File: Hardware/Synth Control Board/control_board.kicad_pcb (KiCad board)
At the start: 2 copper layers, 127 x 177.8 mm, 48 parts, among them J1 Conn_01x13, J10 Conn_01x05, J2 Conn_01x03, J3 Conn_01x13, J4 Conn_01x13, J5 Conn_01x02, J6 Conn_01x13, J7 Conn_01x05, J8 Conn_01x05, J9 Conn_01x05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

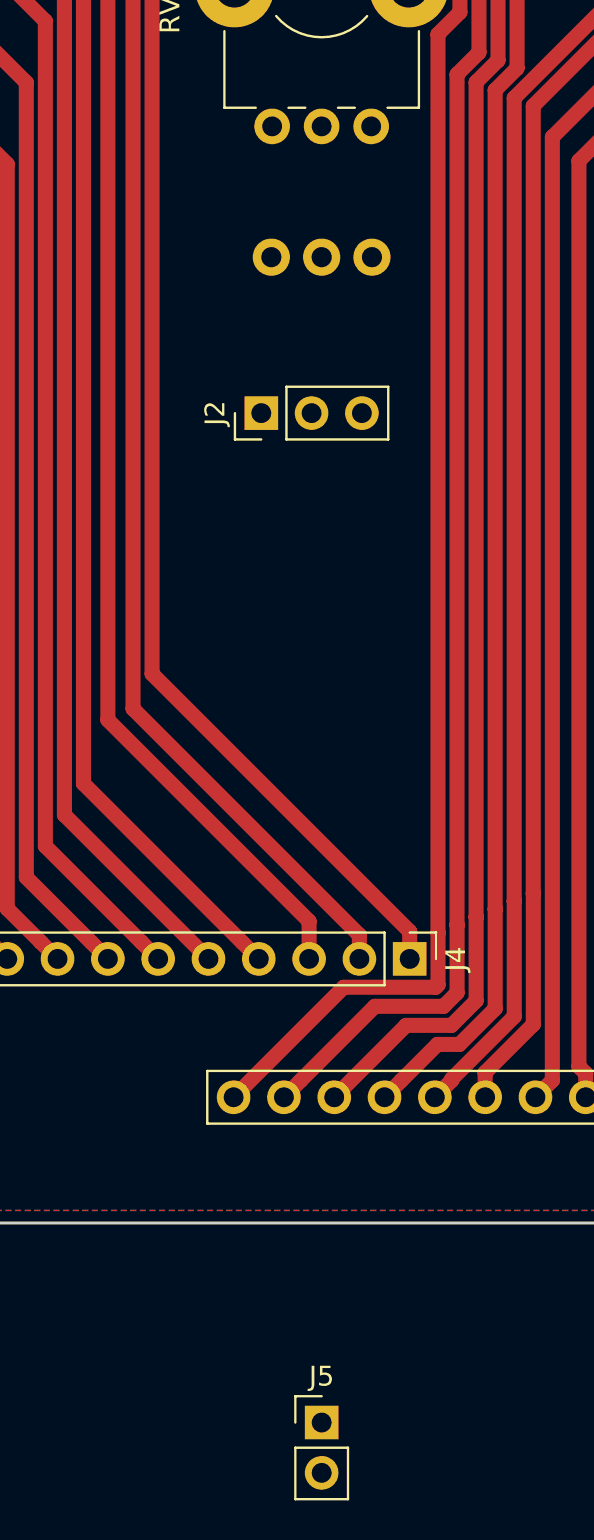
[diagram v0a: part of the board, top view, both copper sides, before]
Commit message: match relative connector placement between two boards
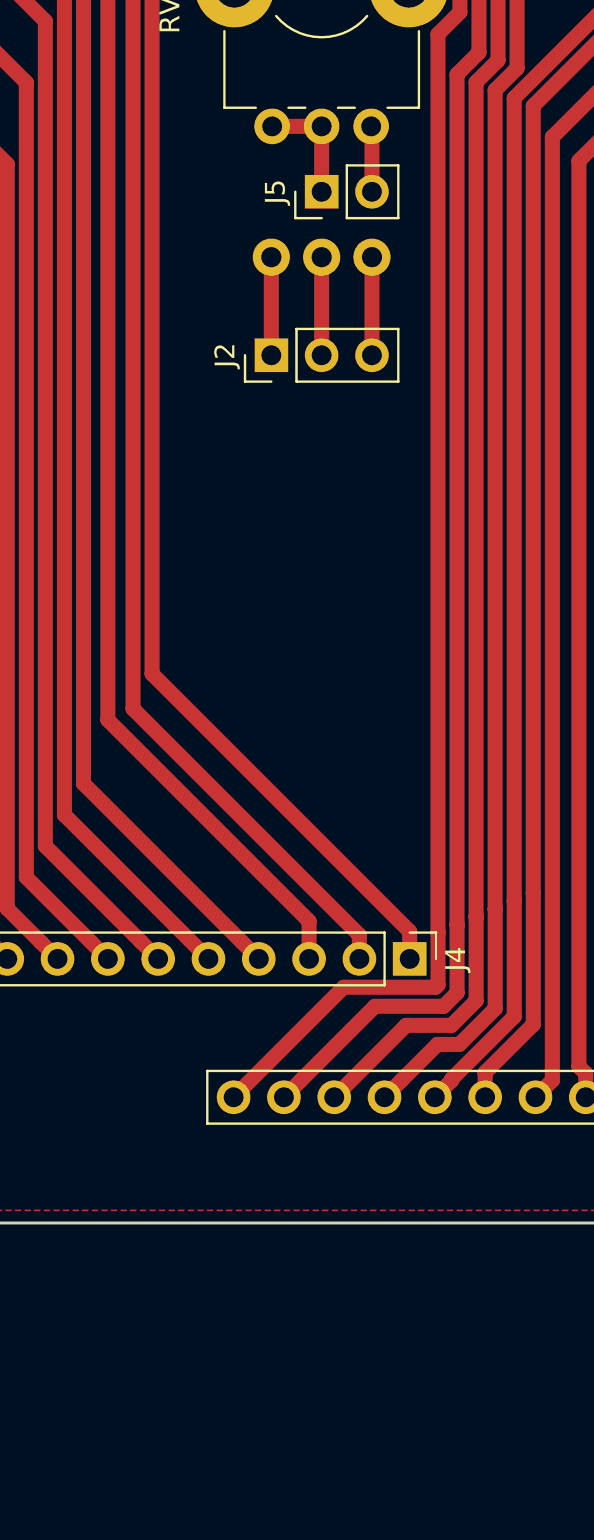
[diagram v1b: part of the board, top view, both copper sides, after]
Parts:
- moved J5 62.1 mm to (63.5, 125.7), turned to 90 degrees
- moved J2 2.96 mm to (61.0, 134.0)
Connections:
- J1 pad 13: GNDD -> GND
- J3 pad 2: GNDD -> GND
- J4 pad 13: GNDD -> GND
- J6 pad 2: GNDD -> GND
- SW10 pad 1: GNDD -> GND
- SW11 pad 1: GNDD -> GND
- SW12 pad 1: GNDD -> GND
- SW13 pad 1: GNDD -> GND
- SW6 pad 2: GNDD -> GND
- SW7 pad 2: GNDD -> GND
- SW8 pad 2: GNDD -> GND
- SW9 pad 2: GNDD -> GND
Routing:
- net /LFO_freq_in: track 0.00 -> 5.80 mm
- net /LFO_tri: track 0.00 -> 4.95 mm
- net /LFO_square: track 0.00 -> 4.95 mm
- net /LFO_out: track 0.00 -> 4.95 mm
- net /LFO_freq_out: track 0.00 -> 3.32 mm

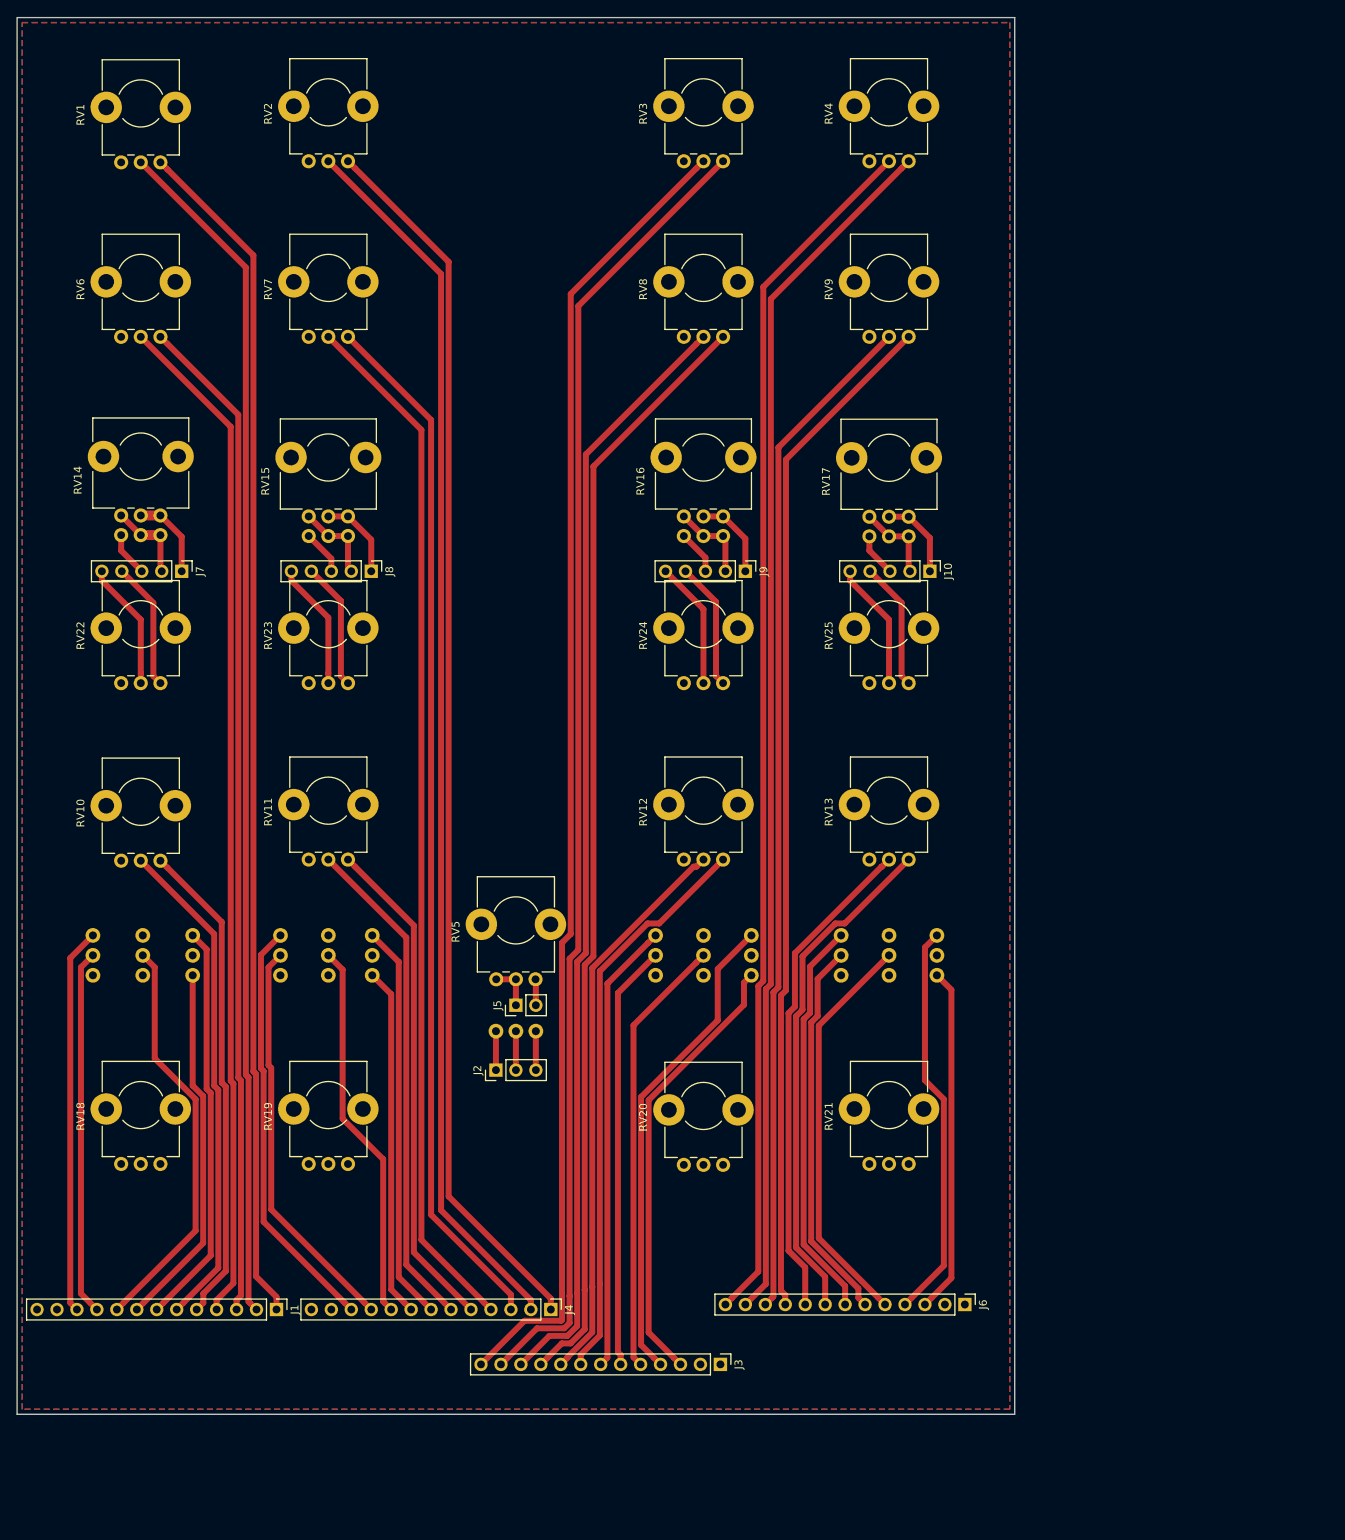
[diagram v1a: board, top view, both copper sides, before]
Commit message: add delay connector to main board and route it.
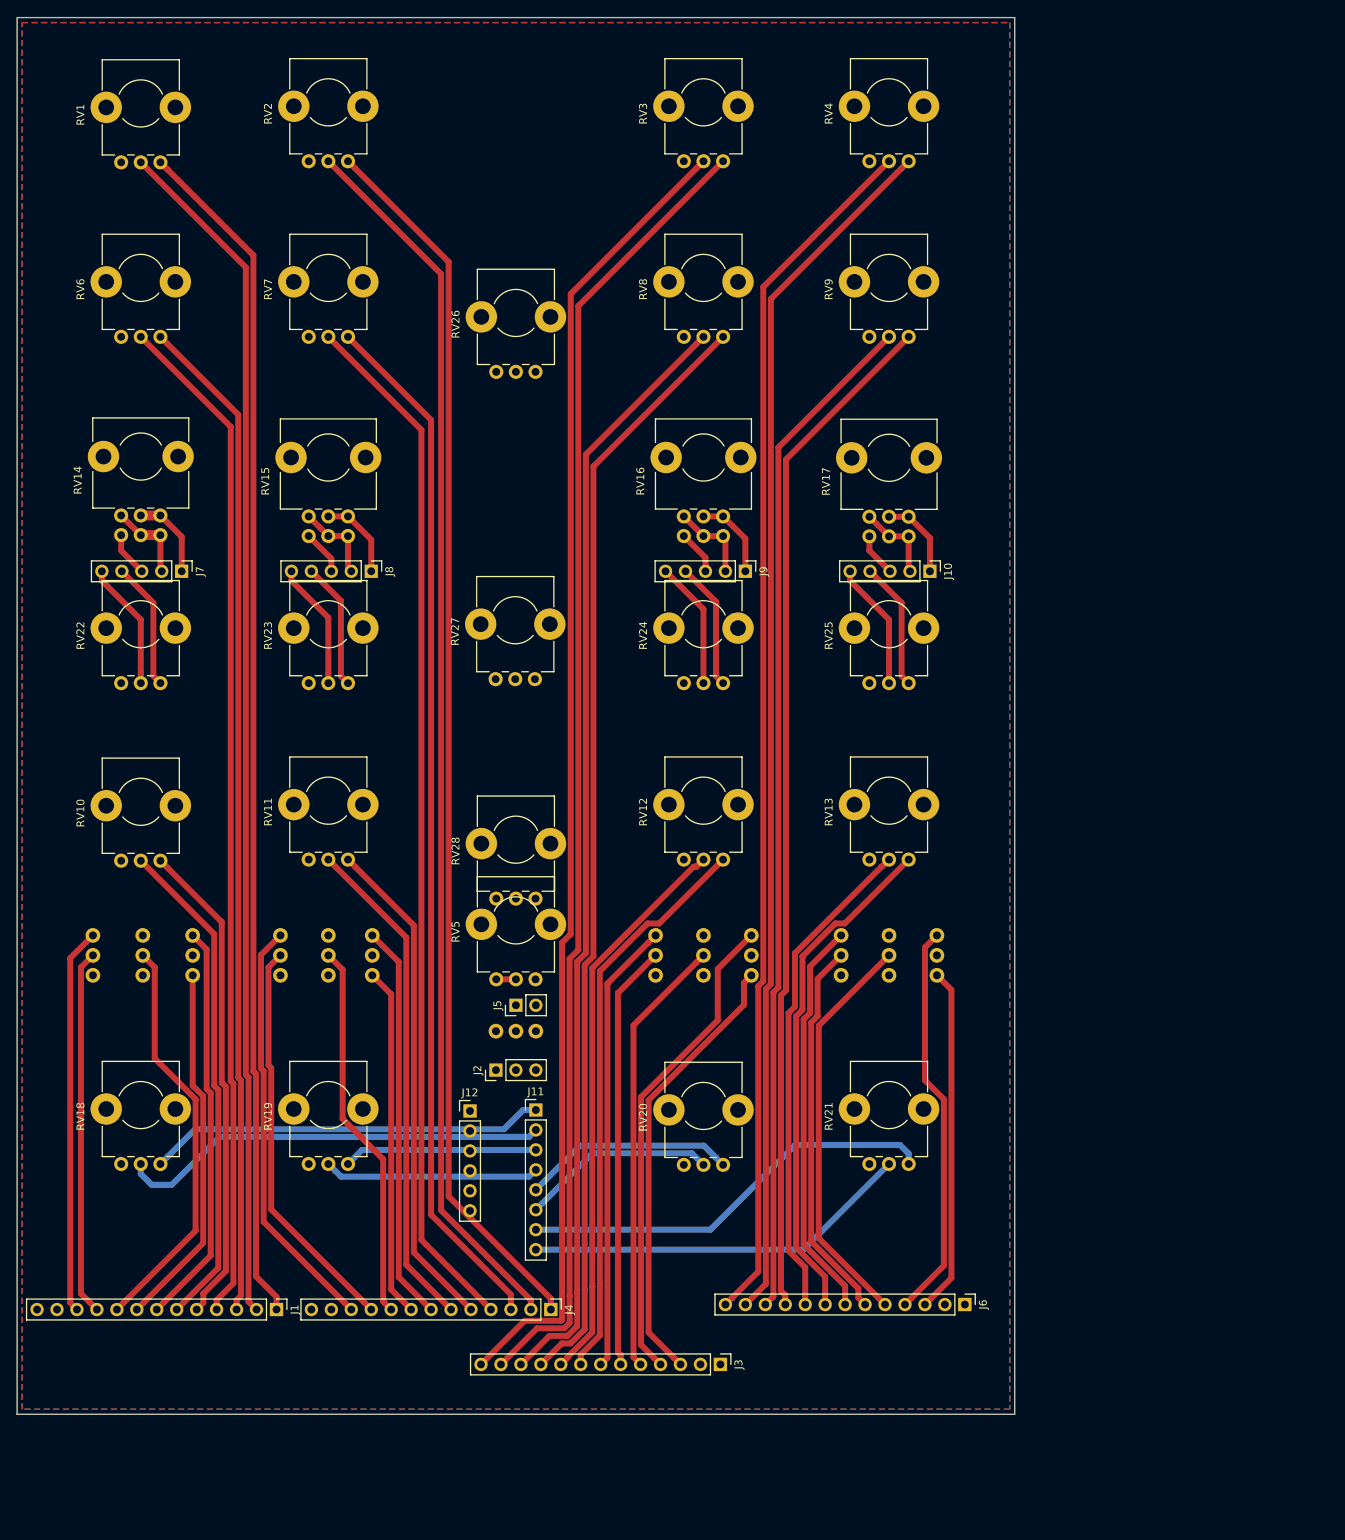
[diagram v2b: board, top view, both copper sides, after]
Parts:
- added J11: Conn_01x08, Pin_Headers:Pin_Header_Straight_1x08_Pitch2.54mm, F.Cu at (66.0, 139.1)
- added J12: Conn_01x06, Pin_Headers:Pin_Header_Straight_1x06_Pitch2.54mm, F.Cu at (57.7, 139.2)
- added RV26: 100kA, Potentiometers:Potentiometer_Bourns_PTV09A-1_Horizontal, F.Cu at (66.0, 45.1)
- added RV27: 100kA, Potentiometers:Potentiometer_Bourns_PTV09A-1_Horizontal, F.Cu at (65.9, 84.2)
- added RV28: 100kA, Potentiometers:Potentiometer_Bourns_PTV09A-1_Horizontal, F.Cu at (66.0, 112.2)
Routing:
- net /vol_out_1: track 0.00 -> 55.0 mm
- net /vol_in_4: track 0.00 -> 53.7 mm
- net /vol_in_1: track 0.00 -> 50.6 mm
- net /vol_out_4: track 0.00 -> 49.5 mm
- net /vol_out_2: track 0.00 -> 27.4 mm
- net /vol_in_3: track 0.00 -> 27.2 mm
- net /vol_out_3: track 0.00 -> 24.9 mm
- net /vol_in_2: track 0.00 -> 24.7 mm
- net /LFO_tri: track 4.95 -> 0.00 mm
- net /LFO_square: track 4.95 -> 0.00 mm
- net /LFO_out: track 4.95 -> 0.00 mm
- net /LFO_freq_in: track 5.80 -> 2.50 mm
- net /LFO_freq_out: track 3.32 -> 0.06 mm
